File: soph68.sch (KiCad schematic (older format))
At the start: 235 parts, among them J1 STLINK_6_Pin, U1 SRV05-4, U2 STM32F072C8Tx, U3 AMS1117-5.0

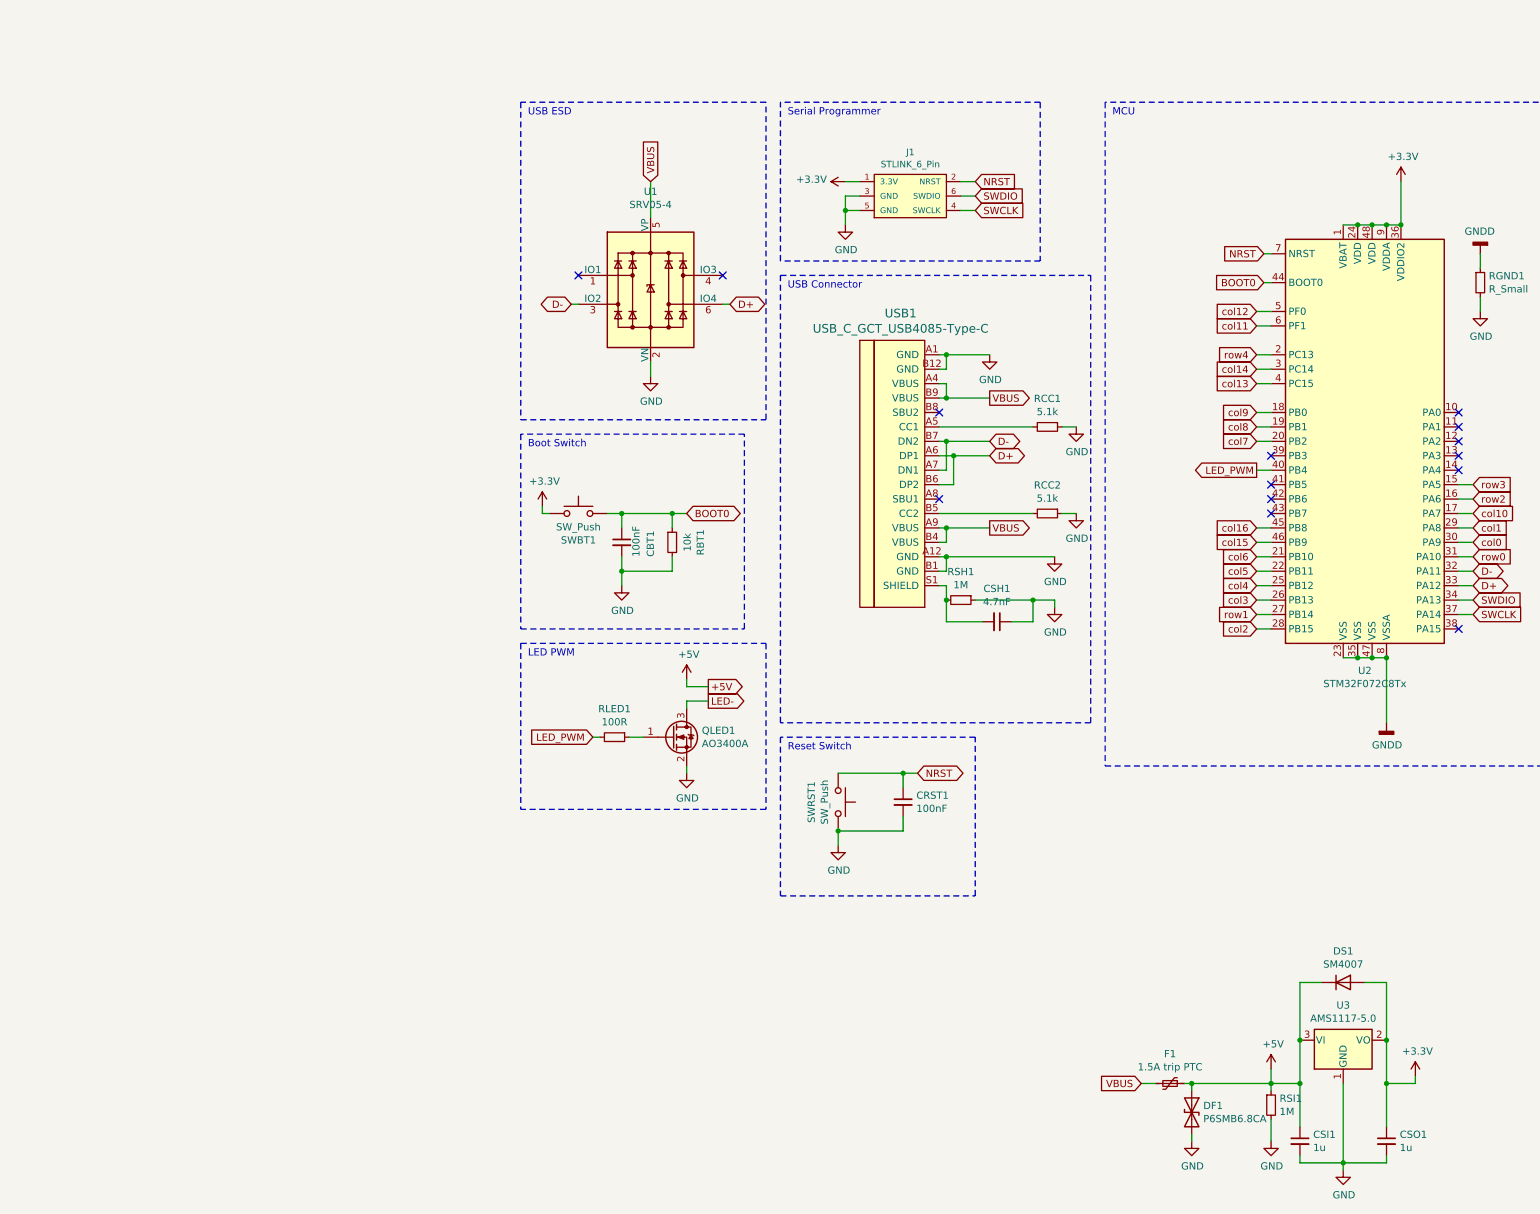
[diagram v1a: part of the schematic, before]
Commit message: Added a box to the power protection biz in the schema
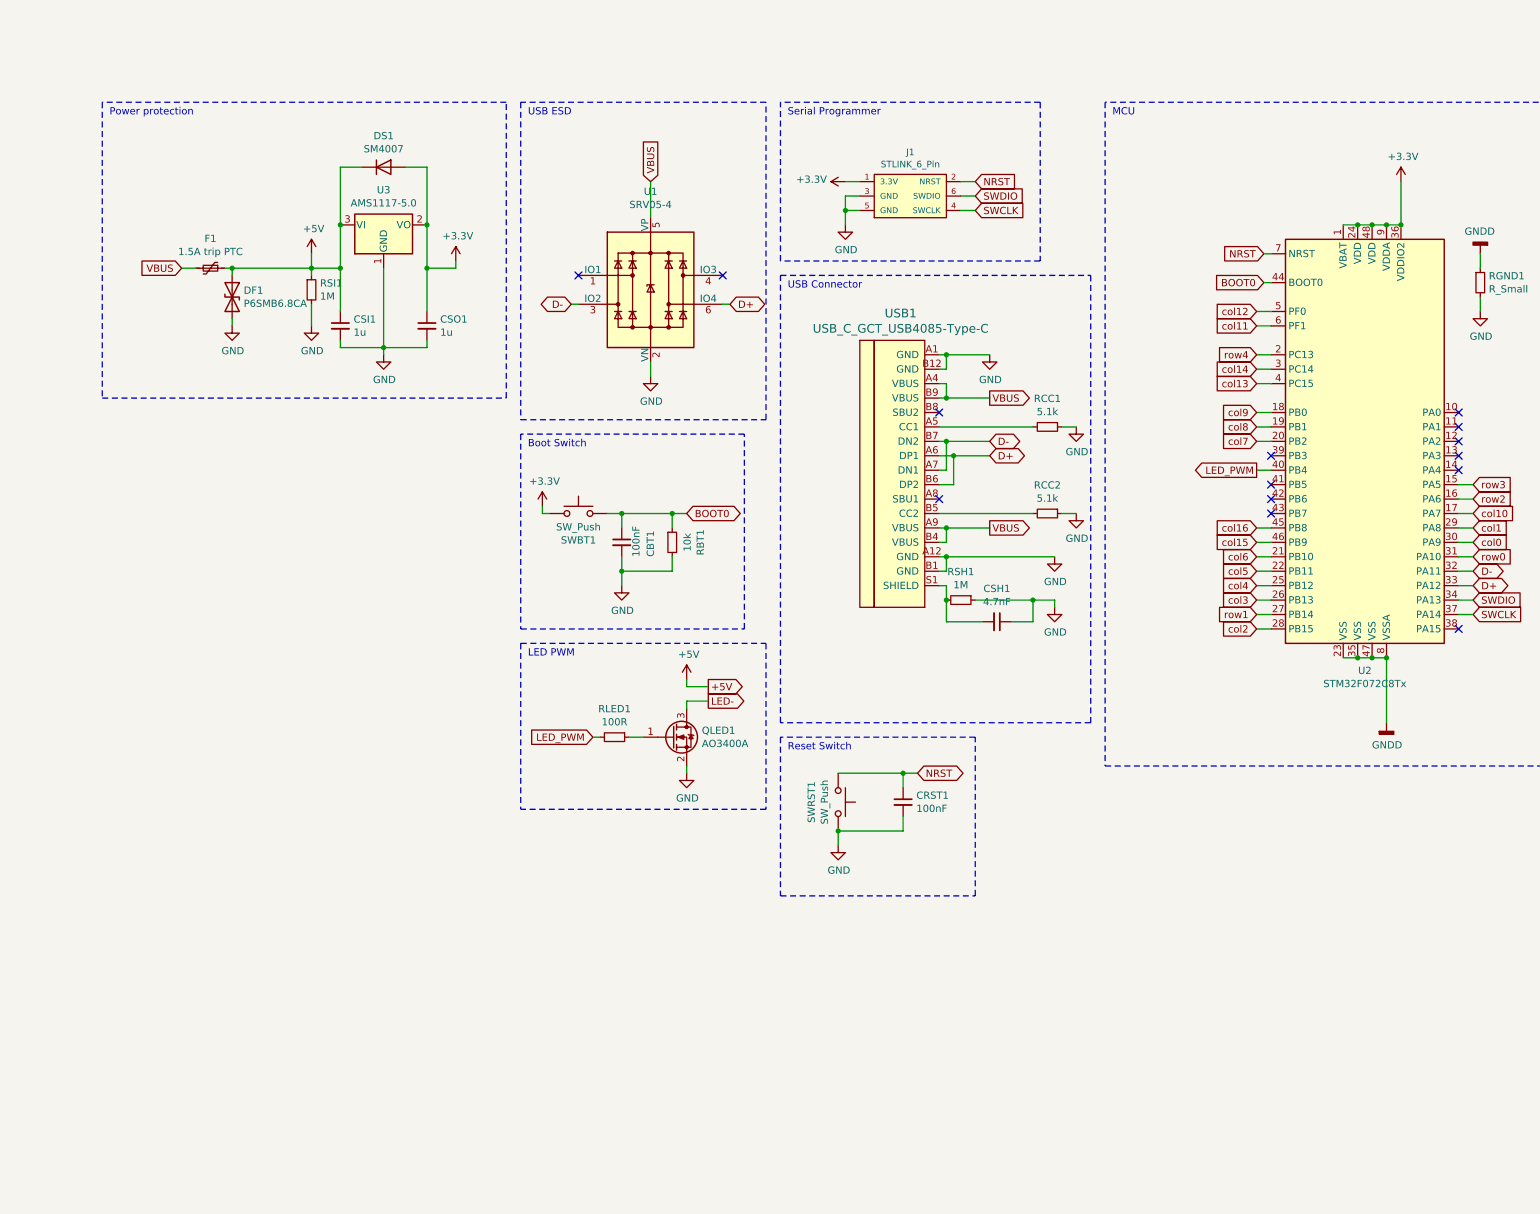
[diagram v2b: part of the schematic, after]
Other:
- note added: "Power protection"
- moved on the sheet: CSI1, CSO1, DF1, DS1, F1, RSI1, U3
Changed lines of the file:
@@
 L Device:Polyfuse_Small F1
 U 1 1 6428420D
-P 15600 13600
-F 0 "F1" V 15395 13600 50  0000 C CNN
-F 1 "1.5A trip PTC" V 15486 13600 50  0000 C CNN
-F 2 "Fuse:Fuse_1812_4532Metric" H 15650 13400 50  0001 L CNN
-F 3 "~" H 15600 13600 50  0001 C CNN
-F 4 "C84140" V 15600 13600 50  0001 C CNN "JLCCode"
-	1    15600 13600
+P 8950 7950
+F 0 "F1" V 8745 7950 50  0000 C CNN
+F 1 "1.5A trip PTC" V 8836 7950 50  0000 C CNN
+F 2 "Fuse:Fuse_1812_4532Metric" H 9000 7750 50  0001 L CNN
+F 3 "~" H 8950 7950 50  0001 C CNN
+F 4 "C84140" V 8950 7950 50  0001 C CNN "JLCCode"
+	1    8950 7950
 	0    1    1    0
 $EndComp
@@
 L Device:D_TVS DF1
 U 1 1 643015E6
-P 15750 13800
-F 0 "DF1" V 15704 13880 50  0000 L CNN
-F 1 "P6SMB6.8CA" V 15795 13880 50  0000 L CNN
-F 2 "Diode_SMD:D_SMB" H 15750 13800 50  0001 C CNN
-F 3 "https://datasheet.lcsc.com/szlcsc/Brightking-Elec-TAIWAN-P6SMB6-8CA_C78395.pdf" H 15750 13800 50  0001 C CNN
-F 4 "C78395" V 15750 13800 50  0001 C CNN "JLCCode"
-	1    15750 13800
+P 9100 8150
+F 0 "DF1" V 9054 8230 50  0000 L CNN
+F 1 "P6SMB6.8CA" V 9145 8230 50  0000 L CNN
+F 2 "Diode_SMD:D_SMB" H 9100 8150 50  0001 C CNN
+F 3 "https://datasheet.lcsc.com/szlcsc/Brightking-Elec-TAIWAN-P6SMB6-8CA_C78395.pdf" H 9100 8150 50  0001 C CNN
+F 4 "C78395" V 9100 8150 50  0001 C CNN "JLCCode"
+	1    9100 8150
 	0    1    1    0
 $EndComp
@@
 L Device:R_Small RSI1
 U 1 1 6430468D
-P 16300 13750
-F 0 "RSI1" H 16359 13796 50  0000 L CNN
-F 1 "1M" H 16359 13705 50  0000 L CNN
-F 2 "Capacitor_SMD:C_0805_2012Metric" H 16300 13750 50  0001 C CNN
-F 3 "~" H 16300 13750 50  0001 C CNN
-F 4 "C17514" H 16300 13750 50  0001 C CNN "JLCCode"
-	1    16300 13750
+P 9650 8100
+F 0 "RSI1" H 9709 8146 50  0000 L CNN
+F 1 "1M" H 9709 8055 50  0000 L CNN
+F 2 "Capacitor_SMD:C_0805_2012Metric" H 9650 8100 50  0001 C CNN
+F 3 "~" H 9650 8100 50  0001 C CNN
+F 4 "C17514" H 9650 8100 50  0001 C CNN "JLCCode"
+	1    9650 8100
 	1    0    0    -1
 $EndComp
@@
 L Device:C_Small CSI1
 U 1 1 64304B64
-P 16500 14000
-F 0 "CSI1" H 16592 14046 50  0000 L CNN
-F 1 "1u" H 16592 13955 50  0000 L CNN
-F 2 "Capacitor_SMD:C_0805_2012Metric" H 16500 14000 50  0001 C CNN
-F 3 "~" H 16500 14000 50  0001 C CNN
-F 4 "C28323" H 16500 14000 50  0001 C CNN "JLCCode"
-	1    16500 14000
+P 9850 8350
+F 0 "CSI1" H 9942 8396 50  0000 L CNN
+F 1 "1u" H 9942 8305 50  0000 L CNN
+F 2 "Capacitor_SMD:C_0805_2012Metric" H 9850 8350 50  0001 C CNN
+F 3 "~" H 9850 8350 50  0001 C CNN
+F 4 "C28323" H 9850 8350 50  0001 C CNN "JLCCode"
+	1    9850 8350
 	1    0    0    -1
 $EndComp
@@
 L Regulator_Linear:AMS1117-5.0 U3
 U 1 1 6430B09C
-P 16800 13300
-F 0 "U3" H 16800 13542 50  0000 C CNN
-F 1 "AMS1117-5.0" H 16800 13451 50  0000 C CNN
-F 2 "Package_TO_SOT_SMD:SOT-223-3_TabPin2" H 16800 13500 50  0001 C CNN
-F 3 "http://www.advanced-monolithic.com/pdf/ds1117.pdf" H 16900 13050 50  0001 C CNN
-F 4 "C6187" H 16800 13300 50  0001 C CNN "JLCCode"
-	1    16800 13300
-	1    0    0    -1
-$EndComp
-Wire Wire Line
-	16500 13300 16500 13600
-Wire Wire Line
-	16500 14150 16500 14100
-Wire Wire Line
-	17100 14150 17100 14100
-Wire Wire Line
-	16300 13600 16300 13650
-Wire Wire Line
-	15750 13600 15750 13650
-Wire Wire Line
-	17100 13600 17300 13600
-Wire Wire Line
-	17300 13600 17300 13550
-Wire Wire Line
-	17100 13600 17100 13300
+P 10150 7650
+F 0 "U3" H 10150 7892 50  0000 C CNN
+F 1 "AMS1117-5.0" H 10150 7801 50  0000 C CNN
+F 2 "Package_TO_SOT_SMD:SOT-223-3_TabPin2" H 10150 7850 50  0001 C CNN
+F 3 "http://www.advanced-monolithic.com/pdf/ds1117.pdf" H 10250 7400 50  0001 C CNN
+F 4 "C6187" H 10150 7650 50  0001 C CNN "JLCCode"
+	1    10150 7650
+	1    0    0    -1
+$EndComp
+Wire Wire Line
+	9850 7650 9850 7950
+Wire Wire Line
+	9850 8500 9850 8450
+Wire Wire Line
+	10450 8500 10450 8450
+Wire Wire Line
+	9650 7950 9650 8000
+Wire Wire Line
+	9100 7950 9100 8000
+Wire Wire Line
+	10450 7950 10650 7950
+Wire Wire Line
+	10650 7950 10650 7900
+Wire Wire Line
+	10450 7950 10450 7650
 $Comp
 L power:+3.3V #PWR0122
 U 1 1 64871062
-P 17300 13550
-F 0 "#PWR0122" H 17300 13400 50  0001 C CNN
-F 1 "+3.3V" H 17315 13723 50  0000 C CNN
-F 2 "" H 17300 13550 50  0001 C CNN
-F 3 "" H 17300 13550 50  0001 C CNN
-	1    17300 13550
-	1    0    0    -1
-$EndComp
-Text GLabel 15400 13600 0    50   Input ~ 0
+P 10650 7900
+F 0 "#PWR0122" H 10650 7750 50  0001 C CNN
+F 1 "+3.3V" H 10665 8073 50  0000 C CNN
+F 2 "" H 10650 7900 50  0001 C CNN
+F 3 "" H 10650 7900 50  0001 C CNN
+	1    10650 7900
+	1    0    0    -1
+$EndComp
+Text GLabel 8750 7950 0    50   Input ~ 0
 VBUS
 Wire Wire Line
-	15400 13600 15500 13600
-Wire Wire Line
-	15700 13600 15750 13600
+	8750 7950 8850 7950
+Wire Wire Line
+	9050 7950 9100 7950
 $Comp
 L power:GND #PWR0123
 U 1 1 649F2D53
-P 16300 14000
-F 0 "#PWR0123" H 16300 13750 50  0001 C CNN
-F 1 "GND" H 16305 13827 50  0000 C CNN
-F 2 "" H 16300 14000 50  0001 C CNN
-F 3 "" H 16300 14000 50  0001 C CNN
-	1    16300 14000
+P 9650 8350
+F 0 "#PWR0123" H 9650 8100 50  0001 C CNN
+F 1 "GND" H 9655 8177 50  0000 C CNN
+F 2 "" H 9650 8350 50  0001 C CNN
+F 3 "" H 9650 8350 50  0001 C CNN
+	1    9650 8350
 	1    0    0    -1
 $EndComp
@@
 L power:GND #PWR0124
 U 1 1 649F47E6
-P 15750 14000
-F 0 "#PWR0124" H 15750 13750 50  0001 C CNN
-F 1 "GND" H 15755 13827 50  0000 C CNN
-F 2 "" H 15750 14000 50  0001 C CNN
-F 3 "" H 15750 14000 50  0001 C CNN
-	1    15750 14000
-	1    0    0    -1
-$EndComp
-Wire Wire Line
-	15750 14000 15750 13950
-Wire Wire Line
-	16300 13850 16300 14000
+P 9100 8350
+F 0 "#PWR0124" H 9100 8100 50  0001 C CNN
+F 1 "GND" H 9105 8177 50  0000 C CNN
+F 2 "" H 9100 8350 50  0001 C CNN
+F 3 "" H 9100 8350 50  0001 C CNN
+	1    9100 8350
+	1    0    0    -1
+$EndComp
+Wire Wire Line
+	9100 8350 9100 8300
+Wire Wire Line
+	9650 8200 9650 8350
 $Comp
 L Diode:SM4007 DS1
 U 1 1 64AF9CA0
-P 16800 12900
-F 0 "DS1" H 16800 13117 50  0000 C CNN
-F 1 "SM4007" H 16800 13026 50  0000 C CNN
-F 2 "Diode_SMD:D_MELF" H 16800 12725 50  0001 C CNN
-F 3 "http://cdn-reichelt.de/documents/datenblatt/A400/SMD1N400%23DIO.pdf" H 16800 12900 50  0001 C CNN
-F 4 "C64898" H 16800 12900 50  0001 C CNN "JLCCode"
-	1    16800 12900
-	1    0    0    -1
-$EndComp
-Wire Wire Line
-	16650 12900 16500 12900
-Wire Wire Line
-	16500 12900 16500 13300
-Connection ~ 16500 13300
-Wire Wire Line
-	16950 12900 17100 12900
-Wire Wire Line
-	17100 12900 17100 13300
-Connection ~ 17100 13300
-Wire Wire Line
-	16500 13600 16500 13900
-Connection ~ 16500 13600
-Wire Wire Line
-	16800 13600 16800 14150
-Wire Wire Line
-	17100 13900 17100 13600
-Connection ~ 17100 13600
+P 10150 7250
+F 0 "DS1" H 10150 7467 50  0000 C CNN
+F 1 "SM4007" H 10150 7376 50  0000 C CNN
+F 2 "Diode_SMD:D_MELF" H 10150 7075 50  0001 C CNN
+F 3 "http://cdn-reichelt.de/documents/datenblatt/A400/SMD1N400%23DIO.pdf" H 10150 7250 50  0001 C CNN
+F 4 "C64898" H 10150 7250 50  0001 C CNN "JLCCode"
+	1    10150 7250
+	1    0    0    -1
+$EndComp
+Wire Wire Line
+	10000 7250 9850 7250
+Wire Wire Line
+	9850 7250 9850 7650
+Connection ~ 9850 7650
+Wire Wire Line
+	10300 7250 10450 7250
+Wire Wire Line
+	10450 7250 10450 7650
+Connection ~ 10450 7650
+Wire Wire Line
+	9850 7950 9850 8250
+Connection ~ 9850 7950
+Wire Wire Line
+	10150 7950 10150 8500
+Wire Wire Line
+	10450 8250 10450 7950
+Connection ~ 10450 7950
 $Comp
 L power:GND #PWR0125
 U 1 1 64E82C95
-P 16800 14200
-F 0 "#PWR0125" H 16800 13950 50  0001 C CNN
-F 1 "GND" H 16805 14027 50  0000 C CNN
-F 2 "" H 16800 14200 50  0001 C CNN
-F 3 "" H 16800 14200 50  0001 C CNN
-	1    16800 14200
+P 10150 8550
+F 0 "#PWR0125" H 10150 8300 50  0001 C CNN
+F 1 "GND" H 10155 8377 50  0000 C CNN
+F 2 "" H 10150 8550 50  0001 C CNN
+F 3 "" H 10150 8550 50  0001 C CNN
+	1    10150 8550
 	1    0    0    -1
 $EndComp
@@
 L Device:C_Small CSO1
 U 1 1 64E87D87
-P 17100 14000
-F 0 "CSO1" H 17192 14046 50  0000 L CNN
-F 1 "1u" H 17192 13955 50  0000 L CNN
-F 2 "Capacitor_SMD:C_0805_2012Metric" H 17100 14000 50  0001 C CNN
-F 3 "~" H 17100 14000 50  0001 C CNN
-F 4 "C28323" H 17100 14000 50  0001 C CNN "JLCCode"
-	1    17100 14000
-	1    0    0    -1
-$EndComp
-Connection ~ 16300 13600
-Wire Wire Line
-	16300 13600 16500 13600
-Connection ~ 15750 13600
-Wire Wire Line
-	15750 13600 16300 13600
+P 10450 8350
+F 0 "CSO1" H 10542 8396 50  0000 L CNN
+F 1 "1u" H 10542 8305 50  0000 L CNN
+F 2 "Capacitor_SMD:C_0805_2012Metric" H 10450 8350 50  0001 C CNN
+F 3 "~" H 10450 8350 50  0001 C CNN
+F 4 "C28323" H 10450 8350 50  0001 C CNN "JLCCode"
+	1    10450 8350
+	1    0    0    -1
+$EndComp
+Connection ~ 9650 7950
+Wire Wire Line
+	9650 7950 9850 7950
+Connection ~ 9100 7950
+Wire Wire Line
+	9100 7950 9650 7950
 Text GLabel 16200 9350 0    50   Output ~ 0
 LED_PWM
@@
 $EndComp
 Wire Wire Line
-	16500 14150 16800 14150
-Connection ~ 16800 14150
-Wire Wire Line
-	16800 14150 16800 14200
-Wire Wire Line
-	16800 14150 17100 14150
+	9850 8500 10150 8500
+Connection ~ 10150 8500
+Wire Wire Line
+	10150 8500 10150 8550
+Wire Wire Line
+	10150 8500 10450 8500
 $Comp
 L power:+5V #PWR0127
 U 1 1 5F197C04
-P 16300 13500
-F 0 "#PWR0127" H 16300 13350 50  0001 C CNN
-F 1 "+5V" H 16315 13673 50  0000 C CNN
-F 2 "" H 16300 13500 50  0001 C CNN
-F 3 "" H 16300 13500 50  0001 C CNN
-	1    16300 13500
-	1    0    0    -1
-$EndComp
-Wire Wire Line
-	16300 13500 16300 13600
+P 9650 7850
+F 0 "#PWR0127" H 9650 7700 50  0001 C CNN
+F 1 "+5V" H 9665 8023 50  0000 C CNN
+F 2 "" H 9650 7850 50  0001 C CNN
+F 3 "" H 9650 7850 50  0001 C CNN
+	1    9650 7850
+	1    0    0    -1
+$EndComp
+Wire Wire Line
+	9650 7850 9650 7950
 $Comp
 L power:+5V #PWR0128
@@
 Wire Wire Line
 	14850 9650 14950 9650
+Wire Notes Line
+	8200 6800 8200 8850
+Wire Notes Line
+	8200 8850 11000 8850
+Wire Notes Line
+	11000 8850 11000 6800
+Wire Notes Line
+	11000 6800 8200 6800
+Text Notes 8250 6900 0    50   ~ 0
+Power protection
 $EndSCHEMATC

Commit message: added jlccode for diodes
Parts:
- D_0, D_1, D_10, D_11, D_12, D_13, D_14, D_15, D_16, D_17, D_18, D_19, D_2, D_20, D_21, D_22, D_23, D_24, D_25, D_26, D_27, D_28, D_3, D_30, D_31, D_32, D_33, D_34, D_35, D_36, D_37, D_38, D_39, D_4, D_40, D_41, D_42, D_43, D_44, D_45, D_46, D_47, D_48, D_49, D_5, D_50, D_51, D_52, D_53, D_54, D_55, D_56, D_57, D_58, D_59, D_6, D_60, D_61, D_62, D_63, D_64, D_65, D_66, D_67, D_7, D_8, D_9: JLCCode (none) -> C81598

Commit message: Changed to cbtx
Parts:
- U2: value STM32F072C8Tx -> STM32F072CBTx; symbol MCU_ST_STM32F0:STM32F072C8Tx -> MCU_ST_STM32F0:STM32F072CBTx; JLCCode (none) -> C81720
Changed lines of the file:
@@
 Connection ~ 17200 7650
 $Comp
-L MCU_ST_STM32F0:STM32F072C8Tx U2
+L MCU_ST_STM32F0:STM32F072CBTx U2
 U 1 1 5EFF243D
 P 17000 9150
 F 0 "U2" H 16950 7561 50  0000 C CNN
-F 1 "STM32F072C8Tx" H 16950 7470 50  0000 C CNN
+F 1 "STM32F072CBTx" H 16950 7470 50  0000 C CNN
 F 2 "Package_QFP:LQFP-48_7x7mm_P0.5mm" H 16400 7750 50  0001 R CNN
 F 3 "http://www.st.com/st-web-ui/static/active/en/resource/technical/document/datasheet/DM00090510.pdf" H 17000 9150 50  0001 C CNN
+F 4 "C81720" H 17000 9150 50  0001 C CNN "JLCCode"
 	1    17000 9150
 	1    0    0    -1
